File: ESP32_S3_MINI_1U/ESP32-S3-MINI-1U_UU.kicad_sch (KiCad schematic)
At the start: 39 parts, among them IC1 TPS6282533DMQR, J1 Castellated_1x07, J2 USB4120-03-C, J3 Qwiic_Vertical, J4 Castellated_1x01, J5 Castellated_1x13, J6 Castellated_1x15, U1 ESP32-S3-MINI-1U, U2 LM66100DCK, U3 LM66100DCK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

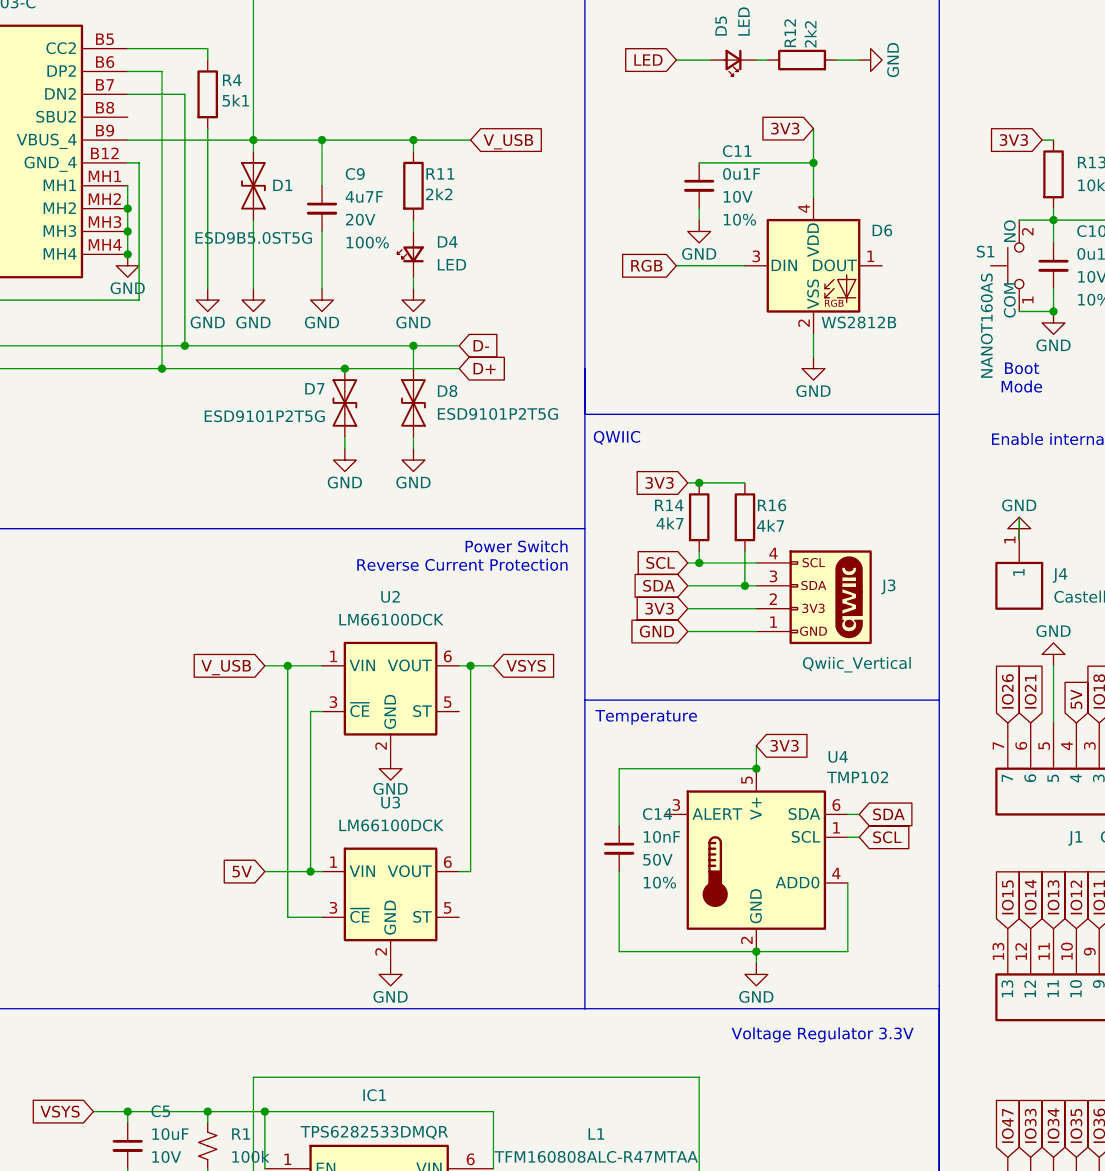
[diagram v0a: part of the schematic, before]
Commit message: Update ESP32 PCB projects and generated assets
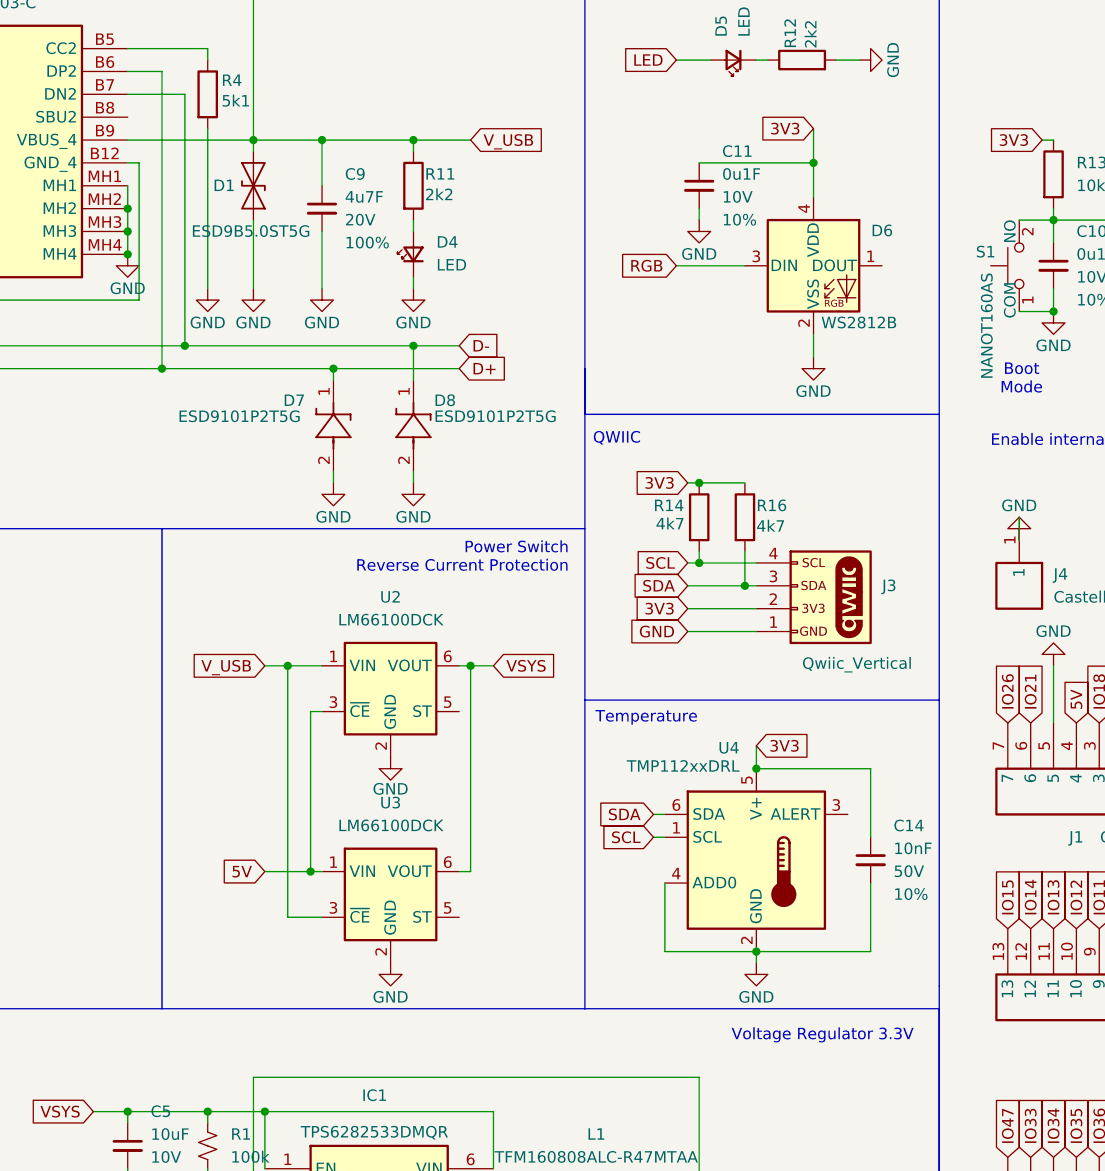
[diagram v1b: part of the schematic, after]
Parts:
- removed U4: TMP102, PCM_SparkFun-Semiconductor-Standard:SOT-563, symbol PCM_SparkFun-Sensor:TMP102
- added U4: TMP112xxDRL, Package_TO_SOT_SMD:SOT-563, symbol Sensor_Temperature:TMP112xxDRL
- D1: footprint Diode_SMD:D_SOD-923 -> ESP32-S3-MINI-1U_Components:SODFL1006X40N
- D7, D8: footprint Diode_SMD:D_SOD-923 -> ESP32-S3-MINI-1U_Components:SODFL1006X40N; symbol Diode:ESD9B5.0ST5G -> ESP32 S3 MINI 1U:ESD9101P2T5G; Arrow Part Number (none) -> ESD9101P2T5G; Arrow Price/Stock (none) -> https://www.arrow.com/en/products/esd9101p2t5g/on-semicondu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; Height (none) -> 0.4; Manufacturer_Name (none) -> onsemi; Manufacturer_Part_Number (none) -> ESD9101P2T5G; Mouser Part Number (none) -> 863-ESD9101P2T5G; Mouser Price/Stock (none) -> https://www.mouser.co.uk/ProductDetail/onsemi/ESD9101P2T5G?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
- IC1: footprint ESP32:TPS6282533DMQR -> ESP32-S3-MINI-1U_Components:TPS6282533DMQR
- J1: footprint Castellated:Castellated_1x07_P2.54mm_D0.80mm -> Castellated_Connectors:Castellated_1x07_P2.54mm_D0.80mm; now left out of the parts list
- J2: footprint ESP32:USB412003C -> ESP32-S3-MINI-1U_Components:USB412003C
- J4: footprint Castellated:Castellated_1x01_P2.54mm_D0.80mm -> Castellated_Connectors:Castellated_1x01_P2.54mm_D0.80mm
- J5: footprint Castellated:Castellated_1x13_P2.54mm_D0.80mm -> Castellated_Connectors:Castellated_1x13_P2.54mm_D0.80mm
- J6: footprint Castellated:Castellated_1x15_P2.54mm_D0.80mm -> Castellated_Connectors:Castellated_1x15_P2.54mm_D0.80mm
- L1: footprint ESP32:INDC1608X75N -> ESP32-S3-MINI-1U_Components:INDC1608X75N
- S1, S2: footprint ESP32:NANOT160AS -> ESP32-S3-MINI-1U_Components:NANOT160AS
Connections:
- net 3V3: now also U4.5 (V+)
- net D+: now also D7.1; no longer D7.2 (A2)
- net D-: now also D8.1; no longer D8.2 (A2)
- net GND: now also D1.2 (A2), D7.2, D8.2, U4.2 (GND), U4.4 (ADD0); no longer D1.1 (A1), D7.1 (A1), D8.1 (A1)
- net SCL: now also U4.1 (SCL)
- net SDA: now also U4.6 (SDA)
- net V_USB: now also D1.1 (A1); no longer D1.2 (A2)
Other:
- title: ESP32-S3-MINI -> ESP32-S3-MINI-1U
- moved on the sheet: C14, D1
